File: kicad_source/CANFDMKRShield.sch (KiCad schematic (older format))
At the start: 13 parts

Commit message: started layout
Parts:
- CN2: renamed from CN?; footprint (none) -> CON_wuerth:WR-TBL_691210910004
- SW1: renamed from SW?; footprint (none) -> mechanical-switches:WE_450404015514
- gave numbers to parts that had none: 11
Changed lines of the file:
@@
 $EndDescr
 $Comp
-L MODULE_compute:ARDUINO_MKR CN?
+L MODULE_compute:ARDUINO_MKR CN1
 U 1 1 5FB0F5B4
 P 4050 6300
-F 0 "CN?" H 4050 7197 60  0000 C CNN
+F 0 "CN1" H 4050 7197 60  0000 C CNN
 F 1 "ARDUINO_MKR" H 4050 7091 60  0000 C CNN
 F 2 "MODULE_compute:ARDUINO_MKR_HOLES" H 3950 6950 60  0001 C CNN
@@
 $EndComp
 $Comp
-L IC_transceiver_can:MCP2517FD U?
+L IC_transceiver_can:MCP2517FD U1
 U 1 1 5FB10D0E
 P 4850 3250
-F 0 "U?" H 4850 3897 60  0000 C CNN
+F 0 "U1" H 4850 3897 60  0000 C CNN
 F 1 "MCP2517FD" H 4850 3791 60  0000 C CNN
 F 2 "SOIC:SOIC-14_3.9x8.7mm_Pitch1.27mm" H 4850 3791 60  0001 C CNN
@@
 $EndComp
 $Comp
-L power-supply:GND #PWR?
+L power-supply:GND #PWR04
 U 1 1 5FB11574
 P 5600 3750
-F 0 "#PWR?" H 5600 3500 50  0001 C CNN
+F 0 "#PWR04" H 5600 3500 50  0001 C CNN
 F 1 "GND" H 5605 3577 50  0000 C CNN
 F 2 "" H 5600 3750 50  0000 C CNN
@@
 $EndComp
 $Comp
-L devices:C_0603 C?
+L devices:C_0603 C1
 U 1 1 5FB120ED
 P 5800 2650
-F 0 "C?" H 5892 2696 50  0000 L CNN
+F 0 "C1" H 5892 2696 50  0000 L CNN
 F 1 "100nF" H 5892 2605 50  0000 L CNN
 F 2 "capacitors:C_0603" H 5800 2500 50  0001 C CNN
@@
 $EndComp
 $Comp
-L devices:Crystal_SMD_4Pad Y?
+L devices:Crystal_SMD_4Pad Y1
 U 1 1 5FB128E3
 P 6200 3650
-F 0 "Y?" H 6200 3870 50  0000 C CNN
+F 0 "Y1" H 6200 3870 50  0000 C CNN
 F 1 "20MHz" H 6200 3779 50  0000 C CNN
 F 2 "crystals:Crystal_SMD_0603_4Pads" H 6200 3450 50  0001 C CNN
@@
 $EndComp
 $Comp
-L power-supply:+3V3 #PWR?
+L power-supply:+3V3 #PWR06
 U 1 1 5FB13272
 P 5800 2450
-F 0 "#PWR?" H 5800 2300 50  0001 C CNN
+F 0 "#PWR06" H 5800 2300 50  0001 C CNN
 F 1 "+3V3" H 5815 2623 50  0000 C CNN
 F 2 "" H 5800 2450 50  0000 C CNN
@@
 $EndComp
 $Comp
-L devices:R_0603 R?
+L devices:R_0603 R3
 U 1 1 5FB14200
 P 9450 3400
-F 0 "R?" H 9509 3446 50  0000 L CNN
+F 0 "R3" H 9509 3446 50  0000 L CNN
 F 1 "120R" H 9509 3355 50  0000 L CNN
 F 2 "resistors:R_0603" H 9450 3250 50  0001 C CNN
@@
 $EndComp
 $Comp
-L devices:C_0603 C?
+L devices:C_0603 C2
 U 1 1 5FB144C3
 P 5850 3850
-F 0 "C?" H 5942 3896 50  0000 L CNN
+F 0 "C2" H 5942 3896 50  0000 L CNN
 F 1 "22pF" H 5942 3805 50  0000 L CNN
 F 2 "capacitors:C_0603" H 5850 3700 50  0001 C CNN
@@
 $EndComp
 $Comp
-L devices:C_0603 C?
+L devices:C_0603 C3
 U 1 1 5FB15897
 P 6550 3850
-F 0 "C?" H 6642 3896 50  0000 L CNN
+F 0 "C3" H 6642 3896 50  0000 L CNN
 F 1 "22pF" H 6642 3805 50  0000 L CNN
 F 2 "capacitors:C_0603" H 6550 3700 50  0001 C CNN
@@
 $EndComp
 $Comp
-L power-supply:GND #PWR?
+L power-supply:GND #PWR08
 U 1 1 5FB15E5D
 P 5850 4000
-F 0 "#PWR?" H 5850 3750 50  0001 C CNN
+F 0 "#PWR08" H 5850 3750 50  0001 C CNN
 F 1 "GND" H 5855 3827 50  0000 C CNN
 F 2 "" H 5850 4000 50  0000 C CNN
@@
 $EndComp
 $Comp
-L power-supply:GND #PWR?
+L power-supply:GND #PWR09
 U 1 1 5FB160EE
 P 6200 4000
-F 0 "#PWR?" H 6200 3750 50  0001 C CNN
+F 0 "#PWR09" H 6200 3750 50  0001 C CNN
 F 1 "GND" H 6205 3827 50  0000 C CNN
 F 2 "" H 6200 4000 50  0000 C CNN
@@
 $EndComp
 $Comp
-L power-supply:GND #PWR?
+L power-supply:GND #PWR010
 U 1 1 5FB1636D
 P 6550 4000
-F 0 "#PWR?" H 6550 3750 50  0001 C CNN
+F 0 "#PWR010" H 6550 3750 50  0001 C CNN
 F 1 "GND" H 6555 3827 50  0000 C CNN
 F 2 "" H 6550 4000 50  0000 C CNN
@@
 $EndComp
 $Comp
-L power-supply:GND #PWR?
+L power-supply:GND #PWR07
 U 1 1 5FB1781D
 P 5800 2800
-F 0 "#PWR?" H 5800 2550 50  0001 C CNN
+F 0 "#PWR07" H 5800 2550 50  0001 C CNN
 F 1 "GND" H 5805 2627 50  0000 C CNN
 F 2 "" H 5800 2800 50  0000 C CNN
@@
 MCP2517_INT
 $Comp
-L power-supply:+3V3 #PWR?
+L power-supply:+3V3 #PWR02
 U 1 1 5FB1D8E4
 P 4750 5550
-F 0 "#PWR?" H 4750 5400 50  0001 C CNN
+F 0 "#PWR02" H 4750 5400 50  0001 C CNN
 F 1 "+3V3" H 4765 5723 50  0000 C CNN
 F 2 "" H 4750 5550 50  0000 C CNN
@@
 $EndComp
 $Comp
-L power-supply:GND #PWR?
+L power-supply:GND #PWR03
 U 1 1 5FB1E67A
 P 4750 7050
-F 0 "#PWR?" H 4750 6800 50  0001 C CNN
+F 0 "#PWR03" H 4750 6800 50  0001 C CNN
 F 1 "GND" H 4755 6877 50  0000 C CNN
 F 2 "" H 4750 7050 50  0000 C CNN
@@
 MCP2517_INT
 $Comp
-L devices:R_0603 R?
+L devices:R_0603 R2
 U 1 1 5FB2791D
 P 5600 6700
-F 0 "R?" H 5659 6746 50  0000 L CNN
+F 0 "R2" H 5659 6746 50  0000 L CNN
 F 1 "10k" H 5659 6655 50  0000 L CNN
 F 2 "resistors:R_0603" H 5600 6550 50  0001 C CNN
@@
 $EndComp
 $Comp
-L power-supply:+3V3 #PWR?
+L power-supply:+3V3 #PWR05
 U 1 1 5FB2889D
 P 5600 6550
-F 0 "#PWR?" H 5600 6400 50  0001 C CNN
+F 0 "#PWR05" H 5600 6400 50  0001 C CNN
 F 1 "+3V3" H 5615 6723 50  0000 C CNN
 F 2 "" H 5600 6550 50  0000 C CNN
@@
 	5600 6850 5750 6850
 $Comp
-L devices:R_0603 R?
+L devices:R_0603 R1
 U 1 1 5FB2AA84
 P 2650 6550
-F 0 "R?" H 2709 6596 50  0000 L CNN
+F 0 "R1" H 2709 6596 50  0000 L CNN
 F 1 "10k" H 2709 6505 50  0000 L CNN
 F 2 "resistors:R_0603" H 2650 6400 50  0001 C CNN
@@
 $EndComp
 $Comp
-L power-supply:+3V3 #PWR?
+L power-supply:+3V3 #PWR01
 U 1 1 5FB2AB46
 P 2650 6400
-F 0 "#PWR?" H 2650 6250 50  0001 C CNN
+F 0 "#PWR01" H 2650 6250 50  0001 C CNN
 F 1 "+3V3" H 2665 6573 50  0000 C CNN
 F 2 "" H 2650 6400 50  0000 C CNN
@@
 NoConn ~ 3450 6950
 $Comp
-L CAN-transceiver:SN65HVD232 U?
+L CAN-transceiver:SN65HVD232 U2
 U 1 1 5FB3525B
 P 7100 3450
-F 0 "U?" H 7625 4337 60  0000 C CNN
+F 0 "U2" H 7625 4337 60  0000 C CNN
 F 1 "SN65HVD232" H 7625 4231 60  0000 C CNN
 F 2 "SOIC:SOIJ-8_5.3x5.3mm_Pitch1.27mm" H 7950 3400 60  0001 C CNN
@@
 	7100 3150 5500 3150
 $Comp
-L mechanical-connectors:CONN_01X04 CN?
+L mechanical-connectors:CONN_01X04 CN2
 U 1 1 5FB37CF3
 P 10300 2800
-F 0 "CN?" H 10378 2841 50  0000 L CNN
+F 0 "CN2" H 10378 2841 50  0000 L CNN
 F 1 "CONN_01X04" H 10378 2750 50  0000 L CNN
-F 2 "" H 10300 2800 50  0000 C CNN
+F 2 "CON_wuerth:WR-TBL_691210910004" H 10300 2800 50  0001 C CNN
 F 3 "" H 10300 2800 50  0000 C CNN
 	1    10300 2800
@@
 	9450 2750 10100 2750
 $Comp
-L devices:C_0603 C?
+L devices:C_0603 C4
 U 1 1 5FB3B8BE
 P 6650 2650
-F 0 "C?" H 6742 2696 50  0000 L CNN
+F 0 "C4" H 6742 2696 50  0000 L CNN
 F 1 "100nF" H 6742 2605 50  0000 L CNN
 F 2 "capacitors:C_0603" H 6650 2500 50  0001 C CNN
@@
 $EndComp
 $Comp
-L power-supply:+3V3 #PWR?
+L power-supply:+3V3 #PWR011
 U 1 1 5FB3BA04
 P 6650 2450
-F 0 "#PWR?" H 6650 2300 50  0001 C CNN
+F 0 "#PWR011" H 6650 2300 50  0001 C CNN
 F 1 "+3V3" H 6665 2623 50  0000 C CNN
 F 2 "" H 6650 2450 50  0000 C CNN
@@
 $EndComp
 $Comp
-L power-supply:GND #PWR?
+L power-supply:GND #PWR012
 U 1 1 5FB3BA0E
 P 6650 2800
-F 0 "#PWR?" H 6650 2550 50  0001 C CNN
+F 0 "#PWR012" H 6650 2550 50  0001 C CNN
 F 1 "GND" H 6655 2627 50  0000 C CNN
 F 2 "" H 6650 2800 50  0000 C CNN
@@
 	6650 2450 6650 2500
 $Comp
-L power-supply:GND #PWR?
+L power-supply:GND #PWR013
 U 1 1 5FB3FC85
 P 7000 3400
-F 0 "#PWR?" H 7000 3150 50  0001 C CNN
+F 0 "#PWR013" H 7000 3150 50  0001 C CNN
 F 1 "GND" H 7005 3227 50  0000 C CNN
 F 2 "" H 7000 3400 50  0000 C CNN
@@
 $EndComp
 $Comp
-L power-supply:GND #PWR?
+L power-supply:GND #PWR015
 U 1 1 5FB40285
 P 10000 3050
-F 0 "#PWR?" H 10000 2800 50  0001 C CNN
+F 0 "#PWR015" H 10000 2800 50  0001 C CNN
 F 1 "GND" H 10005 2877 50  0000 C CNN
 F 2 "" H 10000 3050 50  0000 C CNN
@@
 $EndComp
 $Comp
-L power-supply:VCC #PWR?
+L power-supply:VCC #PWR014
 U 1 1 5FB40D95
 P 9900 2500
-F 0 "#PWR?" H 9900 2350 50  0001 C CNN
+F 0 "#PWR014" H 9900 2350 50  0001 C CNN
 F 1 "VCC" H 9917 2673 50  0000 C CNN
 F 2 "" H 9900 2500 50  0000 C CNN
@@
 CANL
 $Comp
-L devices:SWITCH_SMALL SW?
+L devices:SWITCH_SMALL SW1
 U 1 1 5FB49FCD
 P 9150 3700
-F 0 "SW?" H 9125 4025 50  0000 C CNN
+F 0 "SW1" H 9125 4025 50  0000 C CNN
 F 1 "SWITCH_SMALL" H 9125 3934 50  0000 C CNN
-F 2 "" H 9150 3700 50  0000 C CNN
+F 2 "mechanical-switches:WE_450404015514" H 9150 3700 50  0001 C CNN
 F 3 "" H 9150 3700 50  0000 C CNN
 	1    9150 3700

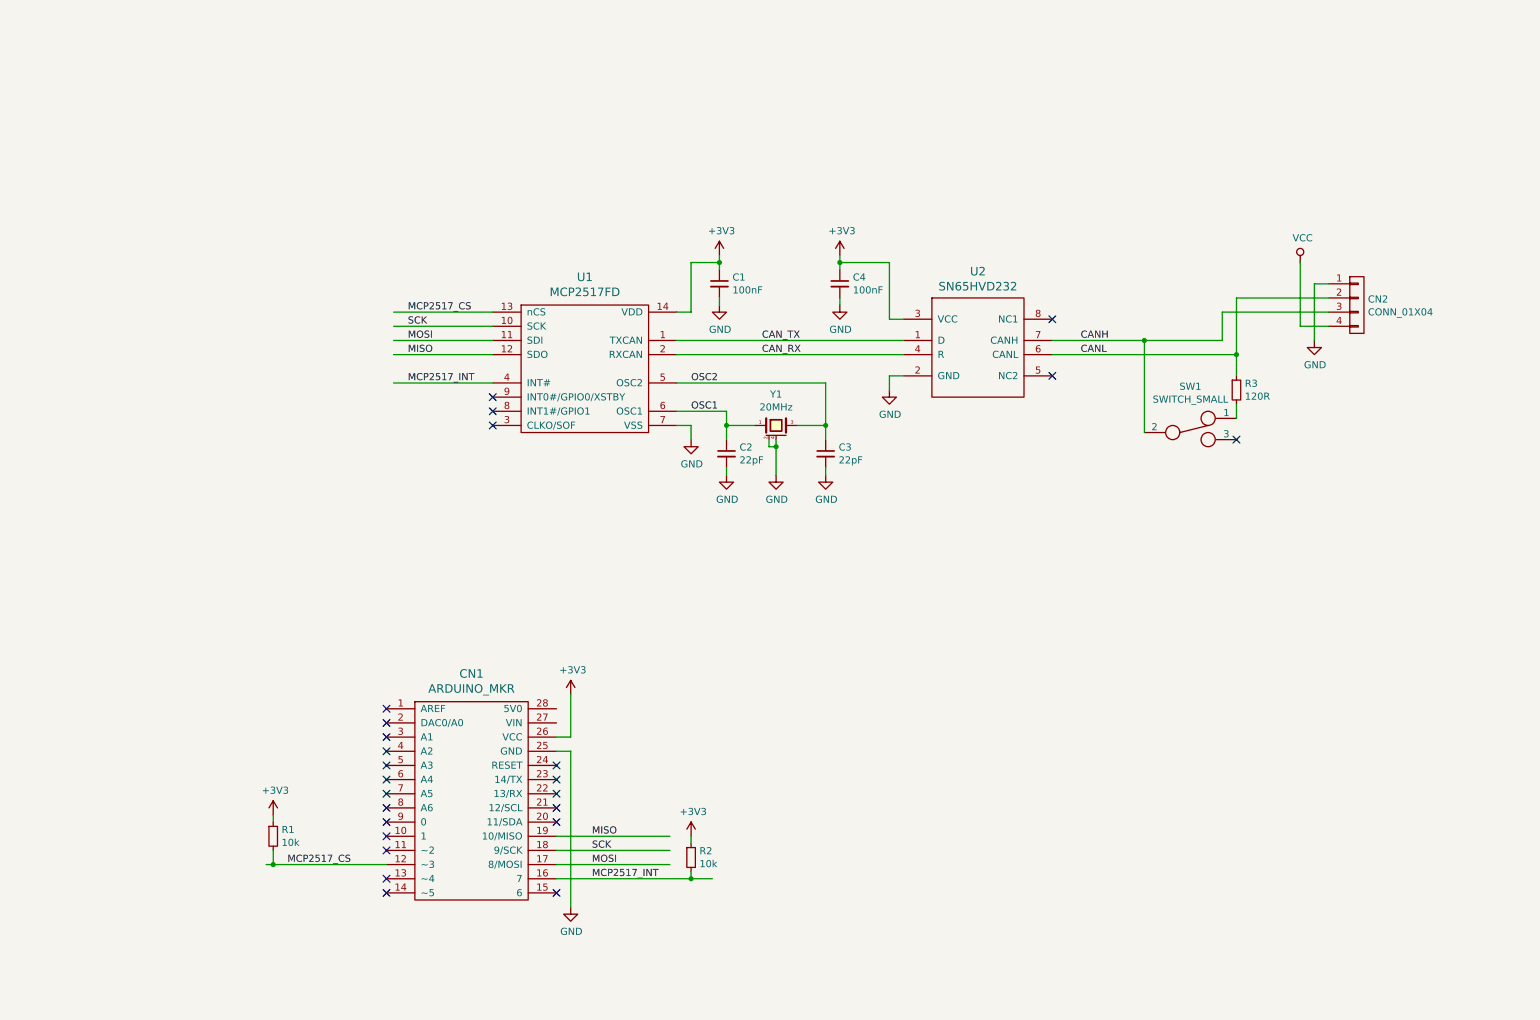
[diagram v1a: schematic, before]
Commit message: added voltage regulators, updated images and pdf schematic
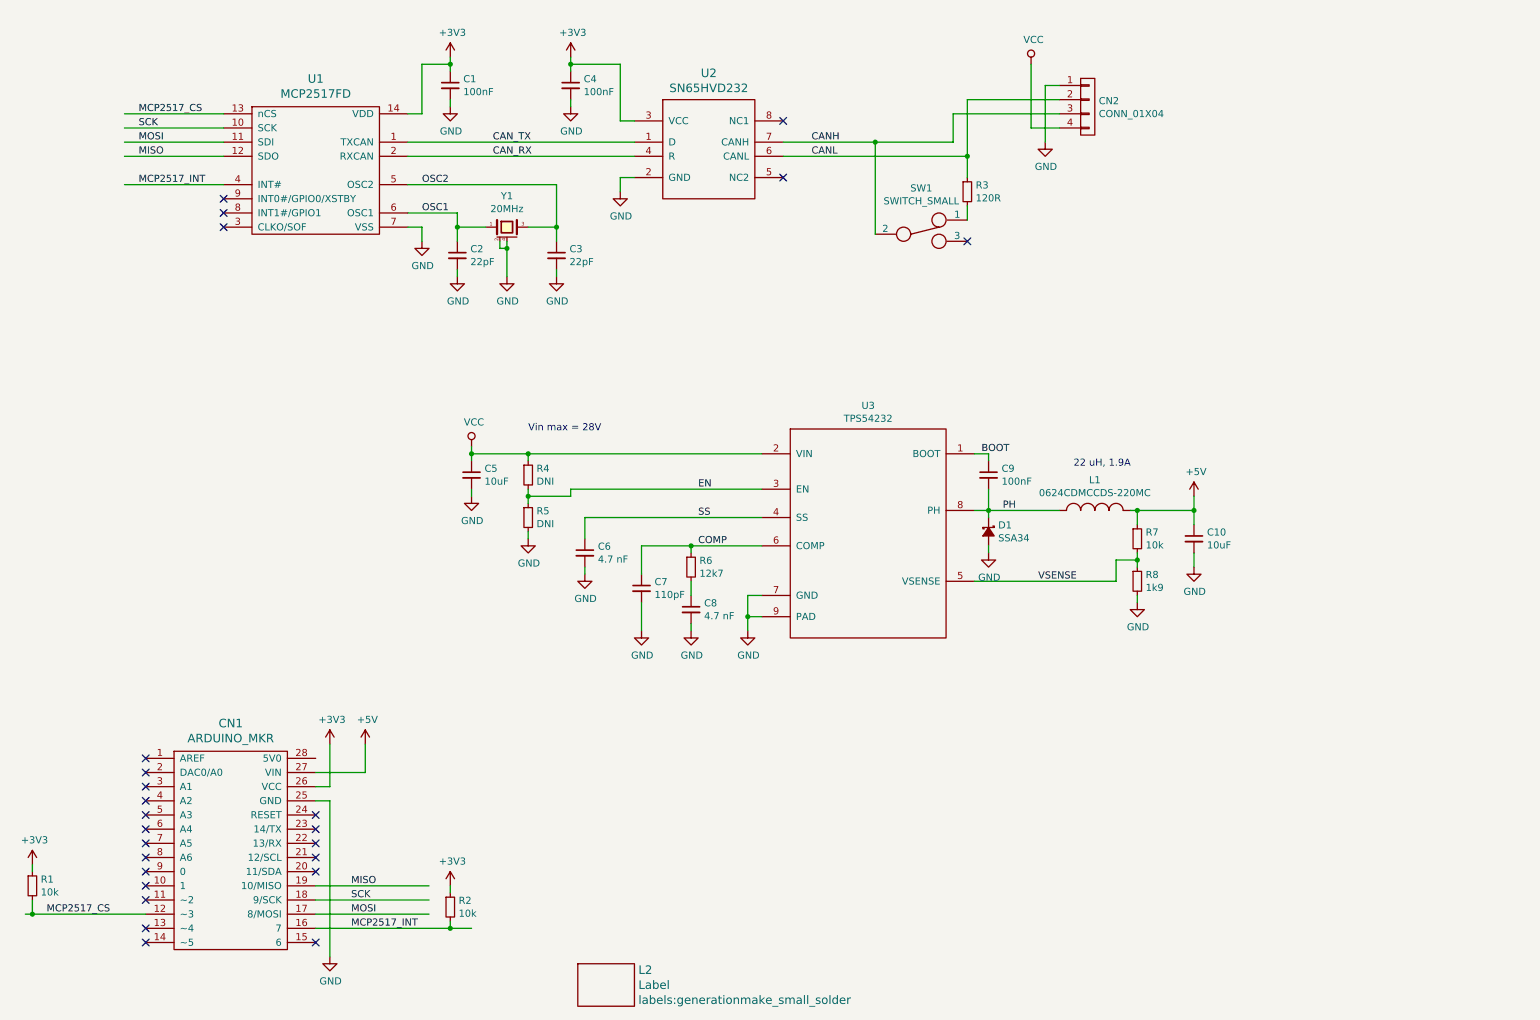
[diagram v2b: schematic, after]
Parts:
- added C10, C5: 10uF, capacitors:C_0805, symbol devices:C_0805
- added C6, C8: 4.7 nF, capacitors:C_0603, symbol devices:C_0603
- added C7: 110pF, capacitors:C_0603, symbol devices:C_0603
- added C9: 100nF, capacitors:C_0603, symbol devices:C_0603
- added D1: SSA34, diodes:SMA_Standard, symbol devices:D_Schottky_Small
- added L1: 0624CDMCCDS-220MC, L_power:Sumida-0624CDMCCDS, symbol devices:INDUCTOR_SMALL
- added L2: Label, labels:generationmake_small_solder, symbol devices:Label
- added R4, R5: DNI, resistors:R_0603, symbol devices:R_0603
- added R6: 12k7, resistors:R_0603, symbol devices:R_0603
- added R7: 10k, resistors:R_0603, symbol devices:R_0603
- added R8: 1k9, resistors:R_0603, symbol devices:R_0603
- added U3: TPS54232, SOIC:SOIC-8-1EP_3.9x4.9mm_Pitch1.27mm, symbol voltage-regulators:TPS54232
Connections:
- net labels added: +5V, BOOT, COMP, EN, PH, SS, VSENSE
- wire segments 66 -> 113
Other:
- note added: "22 uH, 1.9A"
- note added: "Vin max = 28V"
- moved on the sheet: C1, C2, C3, C4, CN1, CN2, R1, R2, R3, SW1, U1, U2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

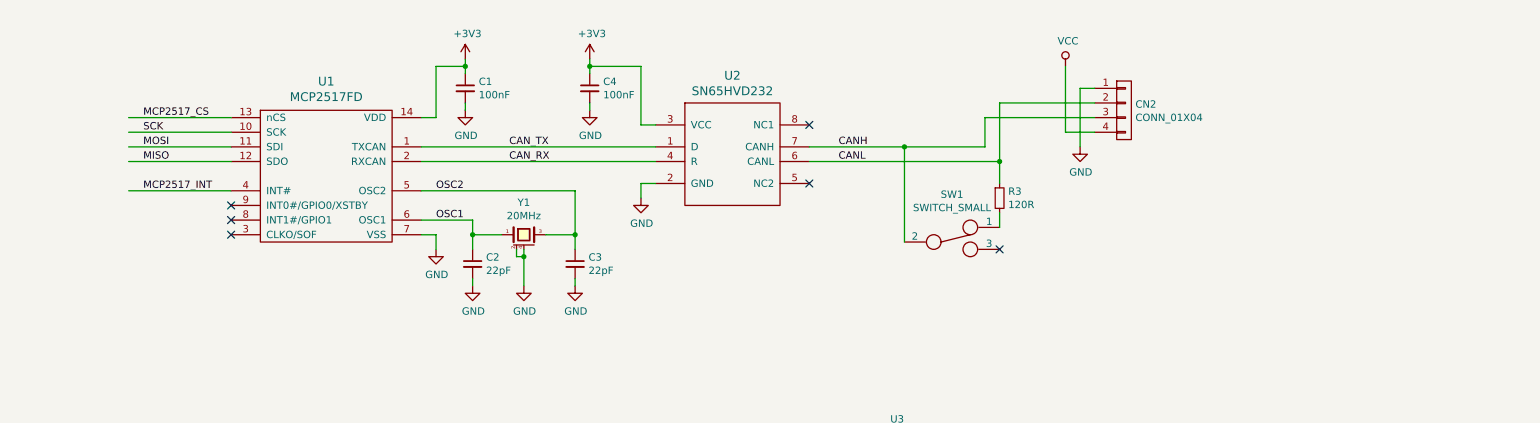
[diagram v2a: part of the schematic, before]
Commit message: added dronecode CAN connectors, updated images and schematic pdf
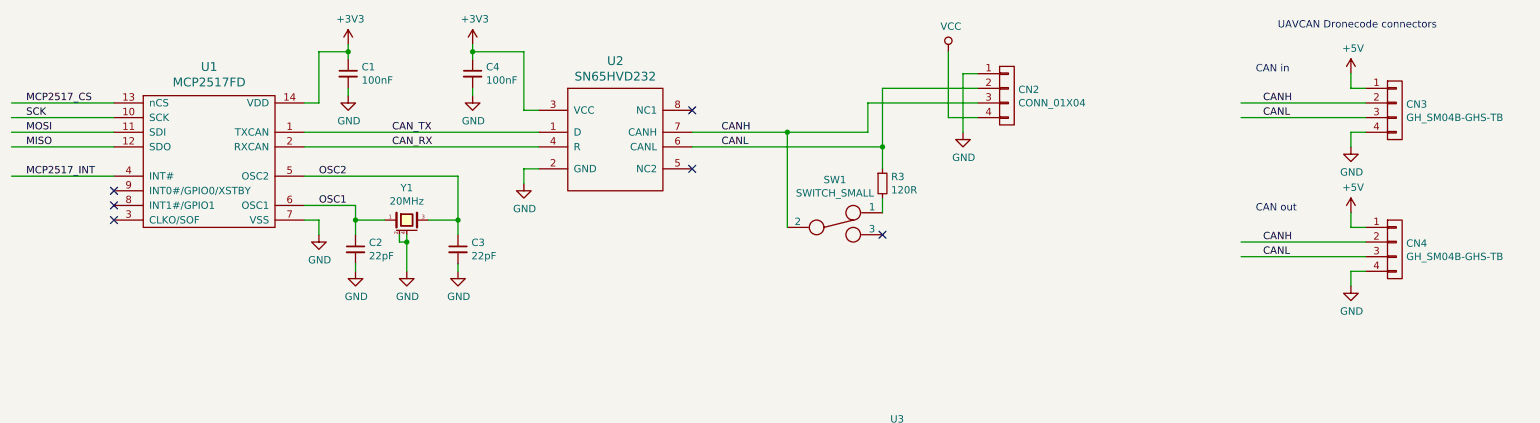
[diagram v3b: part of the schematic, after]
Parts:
- added CN3, CN4: GH_SM04B-GHS-TB, Connector_JST:JST_GH_SM04B-GHS-TB_1x04-1MP_P1.25mm_Horizontal, symbol mechanical-connectors:CONN_01X04
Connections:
- wire segments 113 -> 125
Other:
- note added: "CAN in"
- note added: "CAN out"
- note added: "UAVCAN Dronecode connectors"
- moved on the sheet: C1, C2, C3, C4, CN2, R3, SW1, U1, U2, Y1

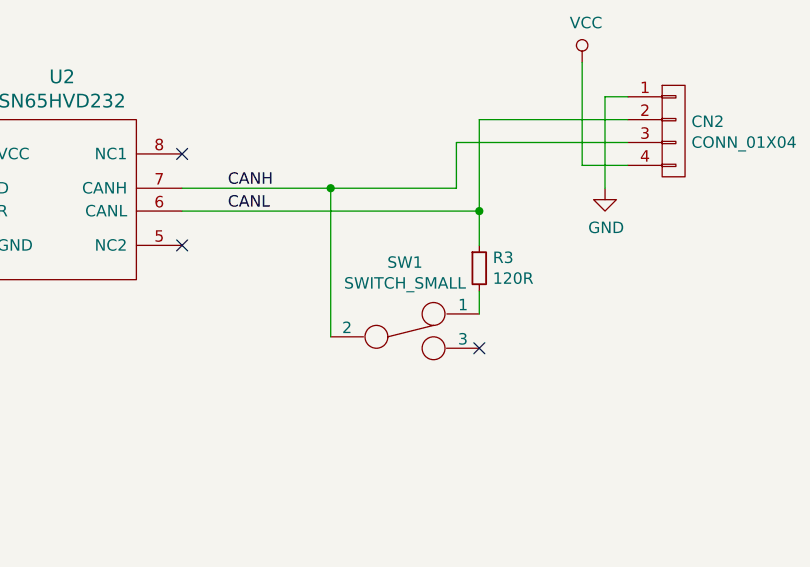
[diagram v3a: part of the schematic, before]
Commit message: updated board shape, changed switch type
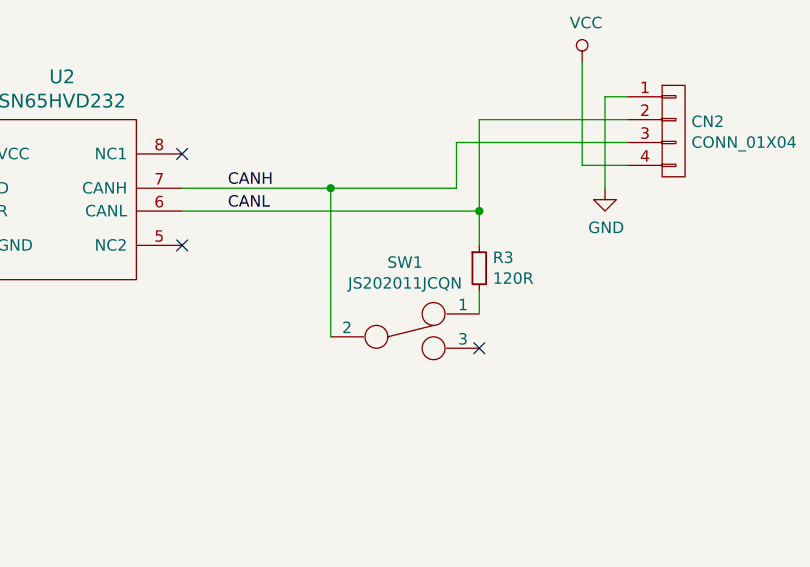
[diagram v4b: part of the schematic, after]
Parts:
- CN1: footprint MODULE_compute:ARDUINO_MKR_HOLES -> MODULE_compute:ARDUINO_MKR_HOLES_PINHEADER_EDGE
- SW1: value SWITCH_SMALL -> JS202011JCQN; footprint mechanical-switches:WE_450404015514 -> mechanical-switches:CK_JS202011JCQN
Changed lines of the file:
@@
 F 0 "CN1" H 2350 7547 60  0000 C CNN
 F 1 "ARDUINO_MKR" H 2350 7441 60  0000 C CNN
-F 2 "MODULE_compute:ARDUINO_MKR_HOLES" H 2250 7300 60  0001 C CNN
+F 2 "MODULE_compute:ARDUINO_MKR_HOLES_PINHEADER_EDGE" H 2250 7300 60  0001 C CNN
 F 3 "" H 2350 6350 60  0000 C CNN
 	1    2350 6650
@@
 P 6450 2200
 F 0 "SW1" H 6425 2525 50  0000 C CNN
-F 1 "SWITCH_SMALL" H 6425 2434 50  0000 C CNN
-F 2 "mechanical-switches:WE_450404015514" H 6450 2200 50  0001 C CNN
+F 1 "JS202011JCQN" H 6425 2434 50  0000 C CNN
+F 2 "mechanical-switches:CK_JS202011JCQN" H 6450 2200 50  0001 C CNN
 F 3 "" H 6450 2200 50  0000 C CNN
 	1    6450 2200
